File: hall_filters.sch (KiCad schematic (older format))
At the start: 11 parts

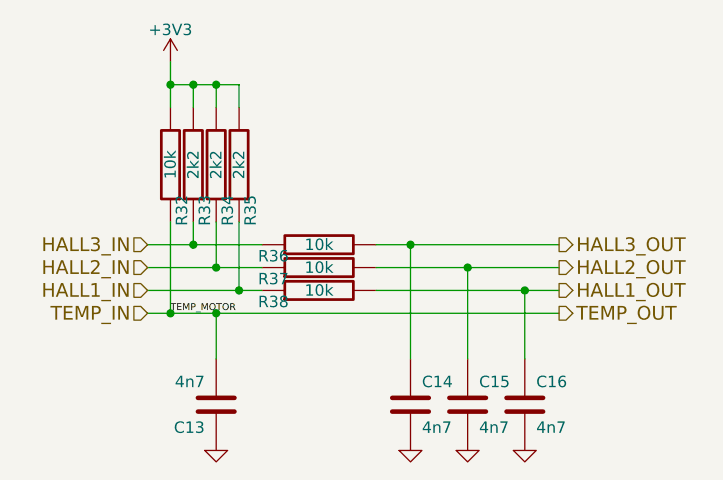
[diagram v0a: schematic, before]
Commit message: - removed 1 MOSFET of each group (no space) - removed 2 DC buffer caps (no space) - power stage routed - shunts and amps routed - post driver routed - pre driver HV routed
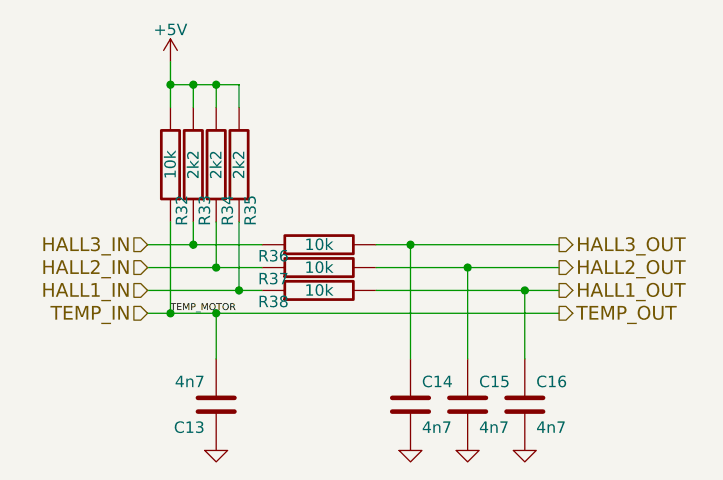
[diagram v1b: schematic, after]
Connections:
- net +3V3 renamed +5V
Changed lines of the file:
@@
 LIBS:contrib
 LIBS:valves
+LIBS:alexlib
 LIBS:Revolter-cache
 EELAYER 25 0
@@
 $EndComp
 $Comp
-L GND-RESCUE-BLDC_4 #PWR034
+L GND-RESCUE-BLDC_4 #PWR030
 U 1 1 53FBB5B2
 P 5950 4450
-F 0 "#PWR034" H 5950 4450 30  0001 C CNN
+F 0 "#PWR030" H 5950 4450 30  0001 C CNN
 F 1 "GND" H 5950 4380 30  0001 C CNN
 F 2 "" H 5950 4450 60  0001 C CNN
@@
 $EndComp
 $Comp
-L GND-RESCUE-BLDC_4 #PWR035
+L GND-RESCUE-BLDC_4 #PWR031
 U 1 1 53FBB5D4
 P 5100 4450
-F 0 "#PWR035" H 5100 4450 30  0001 C CNN
+F 0 "#PWR031" H 5100 4450 30  0001 C CNN
 F 1 "GND" H 5100 4380 30  0001 C CNN
 F 2 "" H 5100 4450 60  0001 C CNN
@@
 	5100 3850 5100 4050
 $Comp
-L GND-RESCUE-BLDC_4 #PWR036
+L GND-RESCUE-BLDC_4 #PWR032
 U 1 1 53FBB5F9
 P 6200 4450
-F 0 "#PWR036" H 6200 4450 30  0001 C CNN
+F 0 "#PWR032" H 6200 4450 30  0001 C CNN
 F 1 "GND" H 6200 4380 30  0001 C CNN
 F 2 "" H 6200 4450 60  0001 C CNN
@@
 $EndComp
 $Comp
-L GND-RESCUE-BLDC_4 #PWR037
+L GND-RESCUE-BLDC_4 #PWR033
 U 1 1 53FBB5FF
 P 6450 4450
-F 0 "#PWR037" H 6450 4450 30  0001 C CNN
+F 0 "#PWR033" H 6450 4450 30  0001 C CNN
 F 1 "GND" H 6450 4380 30  0001 C CNN
 F 2 "" H 6450 4450 60  0001 C CNN
@@
 Text HLabel 6600 3850 2    60   Output ~ 0
 TEMP_OUT
-$Comp
-L +3V3 #PWR038
-U 1 1 5752258C
+Connection ~ 4900 2850
+$Comp
+L +5V #PWR034
+U 1 1 59A345CD
 P 4900 2750
-F 0 "#PWR038" H 4900 2600 50  0001 C CNN
-F 1 "+3V3" H 4900 2890 50  0000 C CNN
-F 2 "" H 4900 2750 60  0000 C CNN
-F 3 "" H 4900 2750 60  0000 C CNN
+F 0 "#PWR034" H 4900 2600 50  0001 C CNN
+F 1 "+5V" H 4900 2890 50  0000 C CNN
+F 2 "" H 4900 2750 50  0000 C CNN
+F 3 "" H 4900 2750 50  0000 C CNN
 	1    4900 2750
 	1    0    0    -1
 $EndComp
-Connection ~ 4900 2850
 $EndSCHEMATC

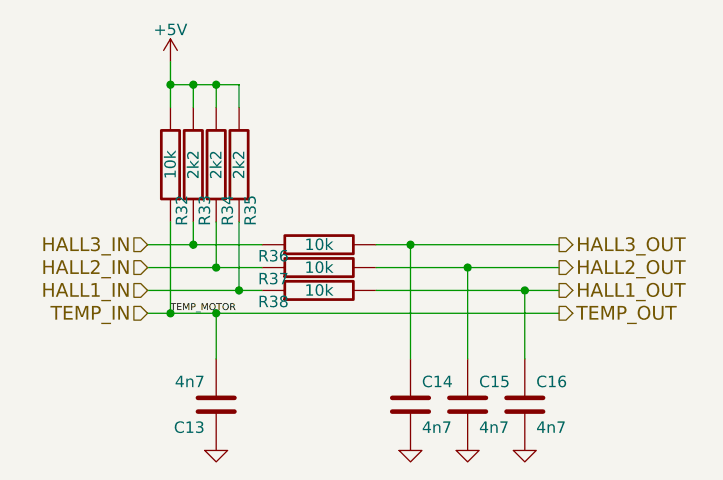
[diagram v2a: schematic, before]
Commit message: - basis commit for V1.1 - did an great overhaul of high current paths - fixed wrong 3V3 reg pin out - blew the IO connector up to 8 pins (turns out 7pin is rare) - changed shunt to 2512 - changed hf caps to double 1210 - two input caps - pin outs for all IO on silk screen - spread the references so you can actually read them - connected the Hall/Temp pull-ups to 3V3 instead of 5V - changed vias to 0.6/0.3mm - changed text to V1.1
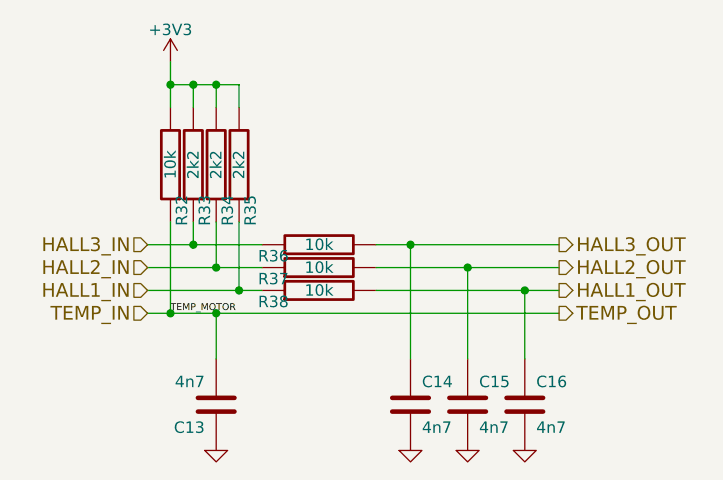
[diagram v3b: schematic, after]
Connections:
- net +5V renamed +3V3
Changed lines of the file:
@@
 $EndComp
 $Comp
-L GND-RESCUE-BLDC_4 #PWR033
+L GND-RESCUE-BLDC_4 #PWR034
 U 1 1 53FBB5B2
 P 5950 4450
-F 0 "#PWR033" H 5950 4450 30  0001 C CNN
+F 0 "#PWR034" H 5950 4450 30  0001 C CNN
 F 1 "GND" H 5950 4380 30  0001 C CNN
 F 2 "" H 5950 4450 60  0001 C CNN
@@
 $EndComp
 $Comp
-L GND-RESCUE-BLDC_4 #PWR034
+L GND-RESCUE-BLDC_4 #PWR035
 U 1 1 53FBB5D4
 P 5100 4450
-F 0 "#PWR034" H 5100 4450 30  0001 C CNN
+F 0 "#PWR035" H 5100 4450 30  0001 C CNN
 F 1 "GND" H 5100 4380 30  0001 C CNN
 F 2 "" H 5100 4450 60  0001 C CNN
@@
 	5100 3850 5100 4050
 $Comp
-L GND-RESCUE-BLDC_4 #PWR035
+L GND-RESCUE-BLDC_4 #PWR036
 U 1 1 53FBB5F9
 P 6200 4450
-F 0 "#PWR035" H 6200 4450 30  0001 C CNN
+F 0 "#PWR036" H 6200 4450 30  0001 C CNN
 F 1 "GND" H 6200 4380 30  0001 C CNN
 F 2 "" H 6200 4450 60  0001 C CNN
@@
 $EndComp
 $Comp
-L GND-RESCUE-BLDC_4 #PWR036
+L GND-RESCUE-BLDC_4 #PWR037
 U 1 1 53FBB5FF
 P 6450 4450
-F 0 "#PWR036" H 6450 4450 30  0001 C CNN
+F 0 "#PWR037" H 6450 4450 30  0001 C CNN
 F 1 "GND" H 6450 4380 30  0001 C CNN
 F 2 "" H 6450 4450 60  0001 C CNN
@@
 Connection ~ 4900 2850
 $Comp
-L +5V #PWR037
-U 1 1 59A345CD
+L +3V3 #PWR038
+U 1 1 5AA50814
 P 4900 2750
-F 0 "#PWR037" H 4900 2600 50  0001 C CNN
-F 1 "+5V" H 4900 2890 50  0000 C CNN
-F 2 "" H 4900 2750 50  0000 C CNN
-F 3 "" H 4900 2750 50  0000 C CNN
+F 0 "#PWR038" H 4900 2600 50  0001 C CNN
+F 1 "+3V3" H 4900 2890 50  0000 C CNN
+F 2 "" H 4900 2750 50  0001 C CNN
+F 3 "" H 4900 2750 50  0001 C CNN
 	1    4900 2750
 	1    0    0    -1

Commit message: - updated project to 5.0.0 - added some more ignores
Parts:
- C13, C14, C15, C16: symbol C-RESCUE-BLDC_4 -> Revolter-rescue:C-RESCUE-BLDC_4
- R32, R33, R34, R35, R36, R37, R38: symbol R-RESCUE-BLDC_4 -> Revolter-rescue:R-RESCUE-BLDC_4
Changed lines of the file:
@@
-EESchema Schematic File Version 2
-LIBS:Revolter-rescue
-LIBS:power
-LIBS:device
-LIBS:transistors
-LIBS:conn
-LIBS:linear
-LIBS:regul
-LIBS:74xx
-LIBS:cmos4000
-LIBS:adc-dac
-LIBS:memory
-LIBS:xilinx
-LIBS:microcontrollers
-LIBS:dsp
-LIBS:microchip
-LIBS:analog_switches
-LIBS:motorola
-LIBS:texas
-LIBS:intel
-LIBS:audio
-LIBS:interface
-LIBS:digital-audio
-LIBS:philips
-LIBS:display
-LIBS:cypress
-LIBS:siliconi
-LIBS:opto
-LIBS:atmel
-LIBS:contrib
-LIBS:valves
-LIBS:alexlib
+EESchema Schematic File Version 4
 LIBS:Revolter-cache
-EELAYER 25 0
+EELAYER 26 0
 EELAYER END
 $Descr A4 11693 8268
@@
 $EndDescr
 $Comp
-L R-RESCUE-BLDC_4 R32
+L Revolter-rescue:R-RESCUE-BLDC_4 R32
 U 1 1 53FBB581
 P 4900 3200
@@
 $EndComp
 $Comp
-L R-RESCUE-BLDC_4 R38
+L Revolter-rescue:R-RESCUE-BLDC_4 R38
 U 1 1 53FBB588
 P 5550 3750
@@
 $EndComp
 $Comp
-L R-RESCUE-BLDC_4 R37
+L Revolter-rescue:R-RESCUE-BLDC_4 R37
 U 1 1 53FBB58F
 P 5550 3650
@@
 $EndComp
 $Comp
-L R-RESCUE-BLDC_4 R36
+L Revolter-rescue:R-RESCUE-BLDC_4 R36
 U 1 1 53FBB596
 P 5550 3550
@@
 $EndComp
 $Comp
-L C-RESCUE-BLDC_4 C14
+L Revolter-rescue:C-RESCUE-BLDC_4 C14
 U 1 1 53FBB59D
 P 5950 4250
@@
 $EndComp
 $Comp
-L C-RESCUE-BLDC_4 C15
+L Revolter-rescue:C-RESCUE-BLDC_4 C15
 U 1 1 53FBB5A4
 P 6200 4250
@@
 $EndComp
 $Comp
-L C-RESCUE-BLDC_4 C16
+L Revolter-rescue:C-RESCUE-BLDC_4 C16
 U 1 1 53FBB5AB
 P 6450 4250
@@
 $EndComp
 $Comp
-L GND-RESCUE-BLDC_4 #PWR034
+L Revolter-rescue:GND-RESCUE-BLDC_4 #PWR034
 U 1 1 53FBB5B2
 P 5950 4450
@@
 $EndComp
 $Comp
-L R-RESCUE-BLDC_4 R33
+L Revolter-rescue:R-RESCUE-BLDC_4 R33
 U 1 1 53FBB5B8
 P 5000 3200
@@
 $EndComp
 $Comp
-L R-RESCUE-BLDC_4 R34
+L Revolter-rescue:R-RESCUE-BLDC_4 R34
 U 1 1 53FBB5BF
 P 5100 3200
@@
 $EndComp
 $Comp
-L R-RESCUE-BLDC_4 R35
+L Revolter-rescue:R-RESCUE-BLDC_4 R35
 U 1 1 53FBB5C6
 P 5200 3200
@@
 $EndComp
 $Comp
-L C-RESCUE-BLDC_4 C13
+L Revolter-rescue:C-RESCUE-BLDC_4 C13
 U 1 1 53FBB5CD
 P 5100 4250
@@
 $EndComp
 $Comp
-L GND-RESCUE-BLDC_4 #PWR035
+L Revolter-rescue:GND-RESCUE-BLDC_4 #PWR035
 U 1 1 53FBB5D4
 P 5100 4450
@@
 	5100 3850 5100 4050
 $Comp
-L GND-RESCUE-BLDC_4 #PWR036
+L Revolter-rescue:GND-RESCUE-BLDC_4 #PWR036
 U 1 1 53FBB5F9
 P 6200 4450
@@
 $EndComp
 $Comp
-L GND-RESCUE-BLDC_4 #PWR037
+L Revolter-rescue:GND-RESCUE-BLDC_4 #PWR037
 U 1 1 53FBB5FF
 P 6450 4450
@@
 Connection ~ 4900 2850
 $Comp
-L +3V3 #PWR038
+L power:+3V3 #PWR038
 U 1 1 5AA50814
 P 4900 2750

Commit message: - swapped TO220 dual MOSFET for single DualCool88 MOSFET package - removed postdriver - changed IRS2110 for IRS2186 - added third shunt - rewired CPU for VESC6 compatibility - layout completely from scratch
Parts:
- C13, C14, C15, C16: footprint Capacitors_SMD:C_0805 -> Capacitor_SMD:C_0805_2012Metric
- R32, R33, R34, R35, R36, R37, R38: footprint Resistors_SMD:R_0805 -> Resistor_SMD:R_0805_2012Metric
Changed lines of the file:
@@
 $Descr A4 11693 8268
 encoding utf-8
-Sheet 4 7
+Sheet 3 7
 Title "HSWR HAL Filters"
 Date "2017-02-05"
@@
 F 0 "R32" V 4850 3400 50  0000 C CNN
 F 1 "10k" V 4900 3200 50  0000 C CNN
-F 2 "Resistors_SMD:R_0805" H 4900 3200 60  0001 C CNN
+F 2 "Resistor_SMD:R_0805_2012Metric" H 4900 3200 60  0001 C CNN
 F 3 "" H 4900 3200 60  0001 C CNN
 	1    4900 3200
@@
 F 0 "R38" V 5500 3950 50  0000 C CNN
 F 1 "10k" V 5550 3750 50  0000 C CNN
-F 2 "Resistors_SMD:R_0805" H 5550 3750 60  0001 C CNN
+F 2 "Resistor_SMD:R_0805_2012Metric" H 5550 3750 60  0001 C CNN
 F 3 "" H 5550 3750 60  0001 C CNN
 	1    5550 3750
@@
 F 0 "R37" V 5500 3850 50  0000 C CNN
 F 1 "10k" V 5550 3650 50  0000 C CNN
-F 2 "Resistors_SMD:R_0805" H 5550 3650 60  0001 C CNN
+F 2 "Resistor_SMD:R_0805_2012Metric" H 5550 3650 60  0001 C CNN
 F 3 "" H 5550 3650 60  0001 C CNN
 	1    5550 3650
@@
 F 0 "R36" V 5500 3750 50  0000 C CNN
 F 1 "10k" V 5550 3550 50  0000 C CNN
-F 2 "Resistors_SMD:R_0805" H 5550 3550 60  0001 C CNN
+F 2 "Resistor_SMD:R_0805_2012Metric" H 5550 3550 60  0001 C CNN
 F 3 "" H 5550 3550 60  0001 C CNN
 	1    5550 3550
@@
 F 0 "C14" H 6000 4350 50  0000 L CNN
 F 1 "4n7" H 6000 4150 50  0000 L CNN
-F 2 "Capacitors_SMD:C_0805" H 5950 4250 60  0001 C CNN
+F 2 "Capacitor_SMD:C_0805_2012Metric" H 5950 4250 60  0001 C CNN
 F 3 "" H 5950 4250 60  0001 C CNN
 	1    5950 4250
@@
 F 0 "C15" H 6250 4350 50  0000 L CNN
 F 1 "4n7" H 6250 4150 50  0000 L CNN
-F 2 "Capacitors_SMD:C_0805" H 6200 4250 60  0001 C CNN
+F 2 "Capacitor_SMD:C_0805_2012Metric" H 6200 4250 60  0001 C CNN
 F 3 "" H 6200 4250 60  0001 C CNN
 	1    6200 4250
@@
 F 0 "C16" H 6500 4350 50  0000 L CNN
 F 1 "4n7" H 6500 4150 50  0000 L CNN
-F 2 "Capacitors_SMD:C_0805" H 6450 4250 60  0001 C CNN
+F 2 "Capacitor_SMD:C_0805_2012Metric" H 6450 4250 60  0001 C CNN
 F 3 "" H 6450 4250 60  0001 C CNN
 	1    6450 4250
@@
 F 0 "R33" V 4950 3400 50  0000 C CNN
 F 1 "2k2" V 5000 3200 50  0000 C CNN
-F 2 "Resistors_SMD:R_0805" H 5000 3200 60  0001 C CNN
+F 2 "Resistor_SMD:R_0805_2012Metric" H 5000 3200 60  0001 C CNN
 F 3 "" H 5000 3200 60  0001 C CNN
 	1    5000 3200
@@
 F 0 "R34" V 5050 3400 50  0000 C CNN
 F 1 "2k2" V 5100 3200 50  0000 C CNN
-F 2 "Resistors_SMD:R_0805" H 5100 3200 60  0001 C CNN
+F 2 "Resistor_SMD:R_0805_2012Metric" H 5100 3200 60  0001 C CNN
 F 3 "" H 5100 3200 60  0001 C CNN
 	1    5100 3200
@@
 F 0 "R35" V 5150 3400 50  0000 C CNN
 F 1 "2k2" V 5200 3200 50  0000 C CNN
-F 2 "Resistors_SMD:R_0805" H 5200 3200 60  0001 C CNN
+F 2 "Resistor_SMD:R_0805_2012Metric" H 5200 3200 60  0001 C CNN
 F 3 "" H 5200 3200 60  0001 C CNN
 	1    5200 3200
@@
 F 0 "C13" H 5150 4350 50  0000 L CNN
 F 1 "4n7" H 5150 4150 50  0000 L CNN
-F 2 "Capacitors_SMD:C_0805" H 5100 4250 60  0001 C CNN
+F 2 "Capacitor_SMD:C_0805_2012Metric" H 5100 4250 60  0001 C CNN
 F 3 "" H 5100 4250 60  0001 C CNN
 	1    5100 4250
@@
 	5200 3450 5200 3750
 Wire Wire Line
-	4800 3750 5300 3750
-Wire Wire Line
-	4800 3650 5300 3650
-Wire Wire Line
-	4800 3550 5300 3550
+	4800 3750 5200 3750
+Wire Wire Line
+	4800 3650 5100 3650
+Wire Wire Line
+	4800 3550 5000 3550
 Wire Wire Line
 	6450 3750 6450 4050
 Wire Wire Line
-	5800 3750 6600 3750
+	5800 3750 6450 3750
 Wire Wire Line
 	6200 3650 6200 4050
 Wire Wire Line
-	5800 3650 6600 3650
+	5800 3650 6200 3650
 Wire Wire Line
 	5950 3550 5950 4050
 Wire Wire Line
-	5800 3550 6600 3550
+	5800 3550 5950 3550
 Wire Wire Line
 	5100 3850 5100 4050
@@
 Connection ~ 4900 3850
 Wire Wire Line
-	4900 2750 4900 2950
-Wire Wire Line
-	4900 2850 5200 2850
+	4900 2750 4900 2850
+Wire Wire Line
+	4900 2850 5000 2850
 Connection ~ 5000 2850
 Connection ~ 5100 2850
 Wire Wire Line
-	4800 3850 6600 3850
+	4800 3850 4900 3850
 Connection ~ 5100 3850
 Text HLabel 4800 3550 0    60   Input ~ 0
@@
 	1    0    0    -1
 $EndComp
+Wire Wire Line
+	5950 3550 6600 3550
+Wire Wire Line
+	6200 3650 6600 3650
+Wire Wire Line
+	6450 3750 6600 3750
+Wire Wire Line
+	5000 3550 5300 3550
+Wire Wire Line
+	5100 3650 5300 3650
+Wire Wire Line
+	5200 3750 5300 3750
+Wire Wire Line
+	4900 3850 5100 3850
+Wire Wire Line
+	5000 2850 5100 2850
+Wire Wire Line
+	5100 2850 5200 2850
+Wire Wire Line
+	5100 3850 6600 3850
+Wire Wire Line
+	4900 2850 4900 2950
 $EndSCHEMATC
